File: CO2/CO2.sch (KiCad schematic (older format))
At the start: 29 parts, among them J1 Conn_Coaxial, J2 Display, J3 SCD30, J4 JST, J5 Conn_Coaxial, Q1 Q_NPN_BCE, U1 NodeMCU1.0(ESP-12E), U2 RFM95W-868S2, U3 MAX-8Q, U4 MCP73831-2-OT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

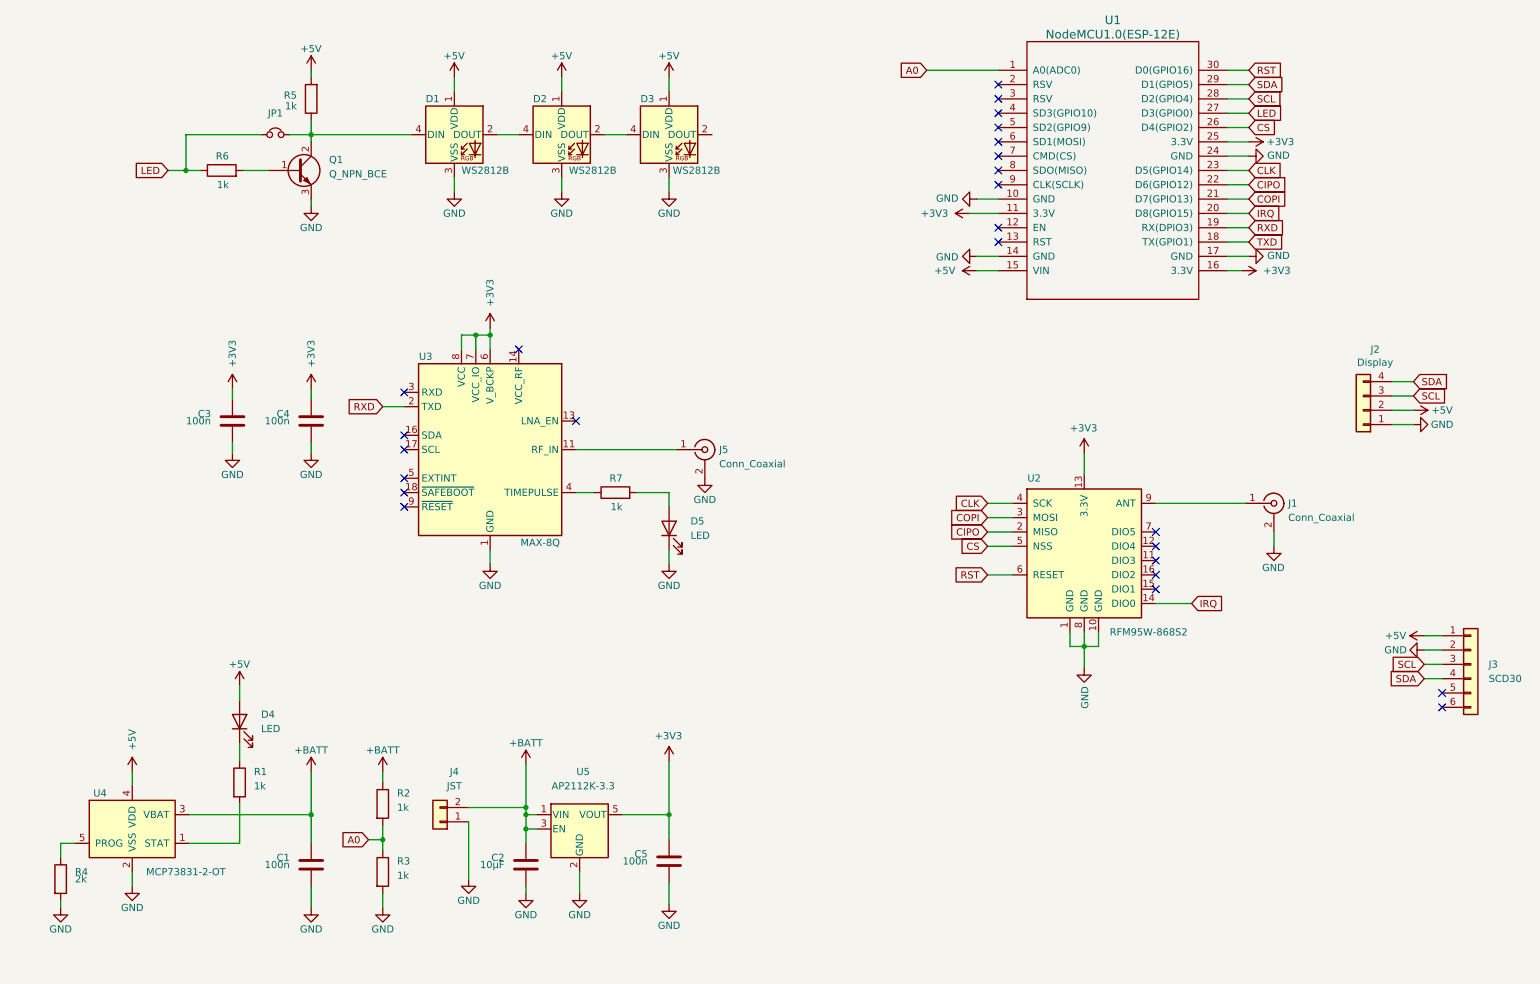
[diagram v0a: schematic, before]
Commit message: add BME680
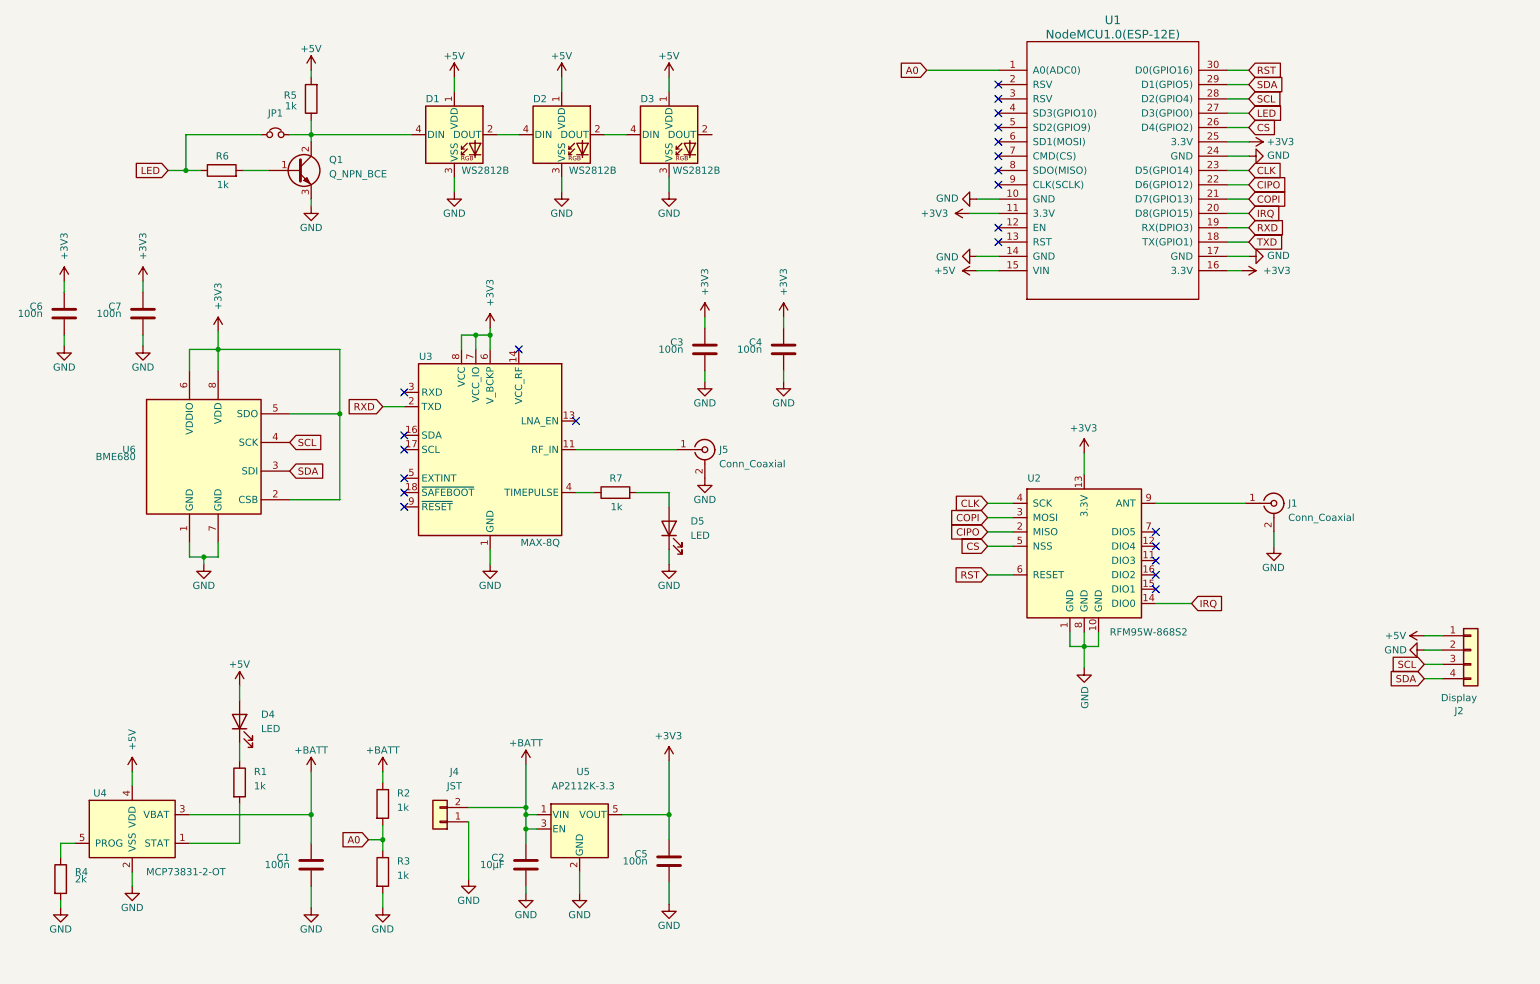
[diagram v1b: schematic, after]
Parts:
- removed J3: SCD30, Connector_PinHeader_2.54mm:PinHeader_1x06_P2.54mm_Vertical, symbol Connector_Generic:Conn_01x06
- added C6, C7: 100n, Capacitor_SMD:C_0603_1608Metric, symbol Device:C
- added U6: BME680, Package_LGA:Bosch_LGA-8_3x3mm_P0.8mm_ClockwisePinNumbering, symbol Sensor:BME680
- C3, C4, D5, J1, J5, R7, U2, U3: Variant (none) -> -CO2,+IOT
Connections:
- net +3V3: now also C6.2, C7.2, U6.2 (CSB), U6.5 (SDO), U6.6 (VDDIO), U6.8 (VDD)
- net +5V: now also J2.1 (Pin_1); no longer J2.2 (Pin_2)
- net GND: now also J2.2 (Pin_2), C6.1, C7.1, U6.1 (GND), U6.7 (GND); no longer J2.1 (Pin_1)
- net SCL: now also U6.4 (SCK)
- net SDA: now also U6.3 (SDI)
- no-connect marks 25 -> 23
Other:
- moved on the sheet: C3, C4, J2

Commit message: do not use this design
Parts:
- removed JP1: Jumper_NC_Small, Jumper:SolderJumper-2_P1.3mm_Open_RoundedPad1.0x1.5mm, symbol CO2-rescue:Jumper_NC_Small-Device-CO2-rescue
- removed Q1: Q_NPN_BCE, Package_TO_SOT_SMD:SOT-23, symbol Device:Q_NPN_BCE
- removed R5, R6: 1k, Resistor_SMD:R_0603_1608Metric, symbol Device:R
- added J3: Micro_SD_Card_Det, Connector_Card:microSD_HC_Molex_104031-0811, symbol Connector:Micro_SD_Card_Det
- added L1: L_Small, Inductor_SMD:L_0402_1005Metric, symbol Device:L_Small
- added R8: 1k, Resistor_SMD:R_0402_1005Metric, symbol Device:R
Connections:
- wire segments 125 -> 121
- no-connect marks 23 -> 22
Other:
- moved on the sheet: C1, C2, C3, C4, C5, D4, J1, J4, R1, R2, R3, R4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
